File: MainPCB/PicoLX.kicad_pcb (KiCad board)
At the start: 2 copper layers, 120.6 x 70.6 mm, 57 parts, among them J1 USB_C_Receptacle_USB2.0, SW1 SW_Push, U1 RP2040, U2 W25Q32JVSS, U3 NCP1117-3.3_SOT223, Y1 12.000MHz

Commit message: Route switches, begin routing LEDs
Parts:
- moved D5 63.7 mm to (159.3, 128.2)
- moved D3 62.3 mm to (103.2, 65.1), turned to -135 degrees
- moved D7 62.3 mm to (215.5, 65.2), turned to 135 degrees
- moved D6 62.3 mm to (215.5, 127.5), turned to 45 degrees
- moved D4 56.2 mm to (103.2, 127.5), turned to -45 degrees
- moved D2 56.2 mm to (159.4, 64.5), turned to 180 degrees
- moved C2 1.87 mm to (191.0, 70.6), turned to 90 degrees
- moved R7 1.06 mm to (192.1, 70.7)
- moved C7 0.86 mm to (191.5, 74.7), turned to 0 degrees
- moved C9 0.80 mm to (191.0, 78.8), turned to -90 degrees
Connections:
- D10 pad 2: Net-(D10-VSS) -> GND
- D10 pad 4: Net-(D10-VDD) -> +5V
- D11 pad 2: Net-(D10-VSS) -> GND
- D11 pad 4: Net-(D10-VDD) -> +5V
- D12 pad 2: Net-(D10-VSS) -> GND
- D12 pad 4: Net-(D10-VDD) -> +5V
- D13 pad 2: Net-(D10-VSS) -> GND
- D13 pad 4: Net-(D10-VDD) -> +5V
- D14 pad 2: Net-(D10-VSS) -> GND
- D14 pad 4: Net-(D10-VDD) -> +5V
- D15 pad 2: Net-(D10-VSS) -> GND
- D15 pad 4: Net-(D10-VDD) -> +5V
- D16 pad 2: Net-(D10-VSS) -> GND
- D16 pad 4: Net-(D10-VDD) -> +5V
- D17 pad 2: Net-(D10-VSS) -> GND
- D17 pad 4: Net-(D10-VDD) -> +5V
- D4 pad 1: unconnected-(D4-DOUT-Pad1) -> Net-(D4-DOUT)
- D5 pad 3: unconnected-(D5-DIN-Pad3) -> Net-(D4-DOUT)
- D8 pad 2: Net-(D10-VSS) -> GND
- D8 pad 4: Net-(D10-VDD) -> +5V
- D9 pad 2: Net-(D10-VSS) -> GND
- D9 pad 4: Net-(D10-VDD) -> +5V
- U1 pad 11: P2 CN -> unconnected-(U1-GPIO8-Pad11)
- U1 pad 12: P2 UR -> unconnected-(U1-GPIO9-Pad12)
- U1 pad 13: P2 DR -> unconnected-(U1-GPIO10-Pad13)
- U1 pad 2: LED ZONE 1 -> P2 UR
- U1 pad 29: unconnected-(U1-GPIO18-Pad29) -> P1 DR
- U1 pad 3: P1 DL -> P2 DR
- U1 pad 30: unconnected-(U1-GPIO19-Pad30) -> P1 DL
- U1 pad 32: unconnected-(U1-GPIO21-Pad32) -> LED ZONE 1
- U1 pad 34: unconnected-(U1-GPIO22-Pad34) -> P1 UR
- U1 pad 35: unconnected-(U1-GPIO23-Pad35) -> P1 CN
- U1 pad 36: unconnected-(U1-GPIO24-Pad36) -> P1 UL
- U1 pad 4: P1 UL -> P2 DL
- U1 pad 5: P1 CN -> P2 CN
- U1 pad 6: P1 UR -> P2 UL
- U1 pad 7: P1 DR -> unconnected-(U1-GPIO5-Pad7)
- U1 pad 8: P2 DL -> unconnected-(U1-GPIO6-Pad8)
- U1 pad 9: P2 UL -> unconnected-(U1-GPIO7-Pad9)
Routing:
- net P1 DL: track 0.00 -> 103.5 mm, vias 0 -> 2
- net P1 CN: track 0.00 -> 92.7 mm, vias 0 -> 2
- net P1 UL: track 0.00 -> 91.8 mm, vias 0 -> 2
- net +3V3: track 27.3 -> 112.5 mm, vias 0 -> 9
- net P2 DL: track 0.00 -> 76.2 mm, vias 0 -> 2
- net P1 DR: track 0.00 -> 65.3 mm, vias 0 -> 2
- net Net-(D3-DOUT): track 0.00 -> 57.6 mm
- net Net-(D6-DOUT): track 0.00 -> 57.4 mm
- net P1 UR: track 0.00 -> 53.8 mm, vias 0 -> 2
- net Net-(D2-DOUT): track 0.00 -> 51.6 mm
- net Net-(D5-DOUT): track 0.00 -> 51.6 mm
- net Net-(D4-DOUT): track 0.00 -> 51.5 mm
- net P2 DR: track 0.00 -> 49.7 mm, vias 0 -> 2
- net P2 CN: track 0.00 -> 46.1 mm, vias 0 -> 2
- net P2 UL: track 0.00 -> 40.8 mm, vias 0 -> 4
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
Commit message: Final functional routing
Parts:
- added C17: 100nF, Capacitor_SMD:C_0402_1005Metric_Pad0.74x0.62mm_HandSolder, B.Cu at (167.9, 63.9)
- added C18: 100uF, Capacitor_SMD:C_0402_1005Metric_Pad0.74x0.62mm_HandSolder, B.Cu at (162.1, 64.5)
- added C19: 100uF, Capacitor_SMD:C_0402_1005Metric_Pad0.74x0.62mm_HandSolder, B.Cu at (105.1, 63.2)
- added C20: 100uF, Capacitor_SMD:C_0402_1005Metric_Pad0.74x0.62mm_HandSolder, B.Cu at (101.3, 125.6)
- added C21: 100uF, Capacitor_SMD:C_0402_1005Metric_Pad0.74x0.62mm_HandSolder, B.Cu at (156.6, 128.2)
- added C22: 100uF, Capacitor_SMD:C_0402_1005Metric_Pad0.74x0.62mm_HandSolder, B.Cu at (213.6, 129.4)
- added C23: 100uF, Capacitor_SMD:C_0402_1005Metric_Pad0.74x0.62mm_HandSolder, B.Cu at (217.4, 67.1)
- added C24: 100uF, Capacitor_SMD:C_0402_1005Metric_Pad0.74x0.62mm_HandSolder, B.Cu at (212.1, 85.0)
- added C25: 100uF, Capacitor_SMD:C_0402_1005Metric_Pad0.74x0.62mm_HandSolder, B.Cu at (212.1, 123.1)
- added C26: 100uF, Capacitor_SMD:C_0402_1005Metric_Pad0.74x0.62mm_HandSolder, B.Cu at (193.0, 104.1)
- added C27: 100uF, Capacitor_SMD:C_0402_1005Metric_Pad0.74x0.62mm_HandSolder, B.Cu at (174.0, 85.0)
- added C28: 100uF, Capacitor_SMD:C_0402_1005Metric_Pad0.74x0.62mm_HandSolder, B.Cu at (173.9, 123.1)
- added C29: 100uF, Capacitor_SMD:C_0402_1005Metric_Pad0.74x0.62mm_HandSolder, B.Cu at (150.1, 85.1)
- added C30: 100uF, Capacitor_SMD:C_0402_1005Metric_Pad0.74x0.62mm_HandSolder, B.Cu at (150.1, 123.1)
- added C31: 100uF, Capacitor_SMD:C_0402_1005Metric_Pad0.74x0.62mm_HandSolder, B.Cu at (131.1, 104.1)
- added C32: 100uF, Capacitor_SMD:C_0402_1005Metric_Pad0.74x0.62mm_HandSolder, B.Cu at (112.1, 123.1)
- added C33: 100uF, Capacitor_SMD:C_0402_1005Metric_Pad0.74x0.62mm_HandSolder, B.Cu at (112.0, 85.0)
- added C34: 100uF, Capacitor_SMD:C_0402_1005Metric_Pad0.74x0.62mm_HandSolder, B.Cu at (168.8, 98.9)
- added C35: 100uF, Capacitor_SMD:C_0402_1005Metric_Pad0.74x0.62mm_HandSolder, B.Cu at (159.6, 98.9)
- added C36: 100uF, Capacitor_SMD:C_0402_1005Metric_Pad0.74x0.62mm_HandSolder, B.Cu at (150.5, 98.9)
- added D18: SK6812MINI, marbastlib-various:LED_6028R, B.Cu at (168.8, 96.3)
- added D19: SK6812MINI, marbastlib-various:LED_6028R, B.Cu at (159.6, 96.3)
- added D20: SK6812MINI, marbastlib-various:LED_6028R, B.Cu at (150.5, 96.3)
- added G***: LOGO, LogoFootprints:Arrow_6, B.Cu at (208.5, 126.9)
- added U4: SN74LV1T34DBV, Package_TO_SOT_SMD:SOT-23-5, B.Cu at (171.5, 64.5)
- moved C15 6.20 mm to (181.6, 90.2), turned to 0 degrees
- moved C16 5.69 mm to (176.0, 88.0), turned to 180 degrees
- moved U3 2.43 mm to (176.6, 93.4), turned to -90 degrees
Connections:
- D11 pad 3: Net-(D10-DOUT) -> Net-(D11-DIN)
- D12 pad 1: Net-(D12-DOUT) -> Net-(D10-DIN)
- D13 pad 3: Net-(D12-DOUT) -> Net-(D13-DIN)
- D14 pad 1: Net-(D14-DOUT) -> Net-(D11-DIN)
- D15 pad 1: Net-(D15-DOUT) -> Net-(D13-DIN)
- D15 pad 3: Net-(D14-DOUT) -> Net-(D15-DIN)
- D16 pad 3: Net-(D15-DOUT) -> LED ZONE 2
- D17 pad 1: LED ZONE 3 -> Net-(D15-DIN)
- D8 pad 3: LED ZONE 2 -> Net-(D10-DOUT)
- D9 pad 1: Net-(D10-DIN) -> LED ZONE 3
- U1 pad 32: LED ZONE 1 -> LED SIGNAL
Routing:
- net +5V: track 52.1 -> 631.6 mm, vias 3 -> 21
- net LED ZONE 3: track 0.00 -> 74.4 mm, vias 0 -> 2
- net Net-(D16-DOUT): track 0.00 -> 44.2 mm, vias 0 -> 2
- net Net-(D11-DOUT): track 0.00 -> 43.6 mm, vias 0 -> 2
- net Net-(D13-DOUT): track 0.00 -> 43.5 mm, vias 0 -> 2
- net Net-(D8-DOUT): track 0.00 -> 41.9 mm, vias 0 -> 2
- net Net-(D10-DOUT): track 0.00 -> 28.5 mm
- net LED ZONE 1: track 36.3 -> 8.31 mm
- net Net-(D13-DIN): track 0.00 -> 27.4 mm
- net Net-(D15-DIN): track 0.00 -> 27.1 mm, vias 0 -> 2
- net Net-(D10-DIN): track 0.00 -> 27.0 mm, vias 0 -> 2
- net LED SIGNAL: track 0.00 -> 23.8 mm, vias 0 -> 2
- net LED ZONE 2: track 0.00 -> 20.3 mm, vias 0 -> 1
- net Net-(D11-DIN): track 0.00 -> 18.4 mm, vias 0 -> 2
- net +3V3: track 112.5 -> 119.1 mm
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- added copper zone on B.Cu, net +3V3
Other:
- board text added: "PicoLX Rev. 1"
- board text added: "https://github.com/dj505/PicoLX"

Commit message: Add test/service, update widths, fix DRC errors, etc
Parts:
- added J2: Conn_01x03, Connector_PinHeader_2.54mm:PinHeader_1x03_P2.54mm_Vertical, F.Cu at (188.0, 123.0)
- moved G*** 0.97 mm to (208.5, 127.9)
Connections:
- U1 pad 15: unconnected-(U1-GPIO12-Pad15) -> TEST
- U1 pad 16: unconnected-(U1-GPIO13-Pad16) -> SERVICE
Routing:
- net SERVICE: track 0.00 -> 51.1 mm, vias 0 -> 1
- net TEST: track 0.00 -> 50.2 mm, vias 0 -> 1
- net GND: track 31.9 -> 34.8 mm, vias 10 -> 12
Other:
- board text added: "BOOTSEL"
- board text added: "P1 CENTER"
- board text added: "P1 DOWN LEFT"
- board text added: "P1 DOWN RIGHT"
- board text added: "P1 UP LEFT"
- board text added: "P1 UP RIGHT"
- board text added: "P2 CENTER"
- board text added: "P2 DOWN LEFT"
- board text added: "P2 DOWN RIGHT"
- board text added: "P2 UP LEFT"
- board text added: "P2 UP RIGHT"

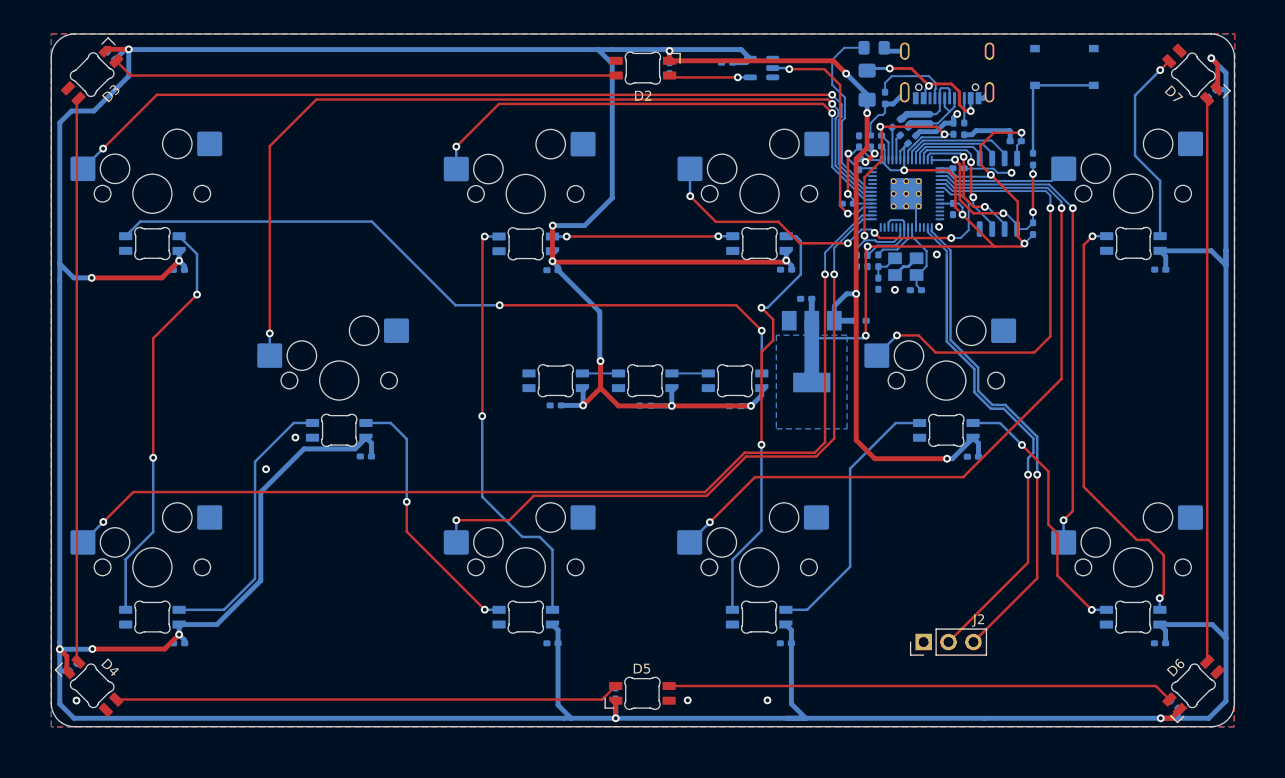
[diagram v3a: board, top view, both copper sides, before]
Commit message: Fix edge clearance and accompanying DRC errors
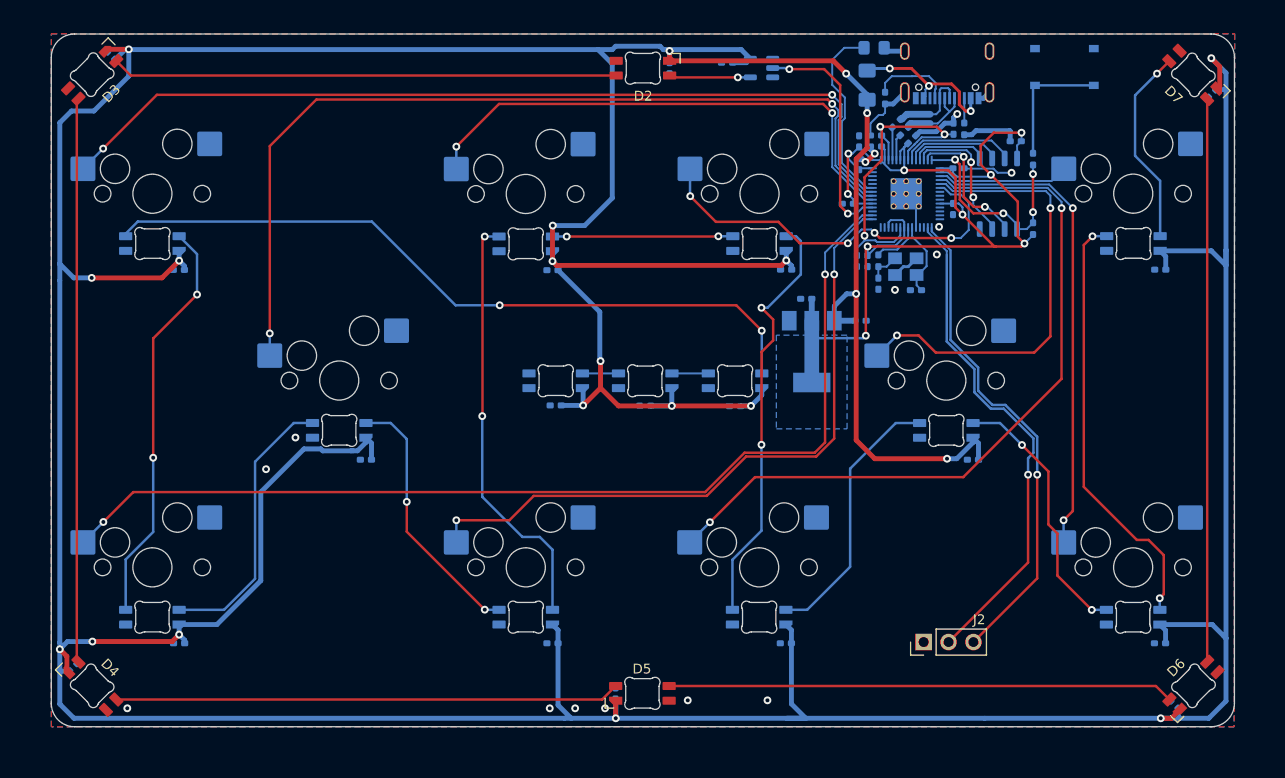
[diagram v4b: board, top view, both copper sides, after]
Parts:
- moved C31 0.33 mm to (131.1, 104.4)
- moved C26 0.30 mm to (193.0, 104.4)
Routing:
- net +5V: track 631.6 -> 633.7 mm
- net GND: vias 12 -> 15
